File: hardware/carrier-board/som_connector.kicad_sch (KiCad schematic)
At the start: 4 parts, among them J1 SS5-80-3.50-L-D-K-TR, J2 SS5-80-3.50-L-D-K-TR, J3 SS5-80-3.50-L-D-K-TR, J4 SS5-80-3.50-L-D-K-TR

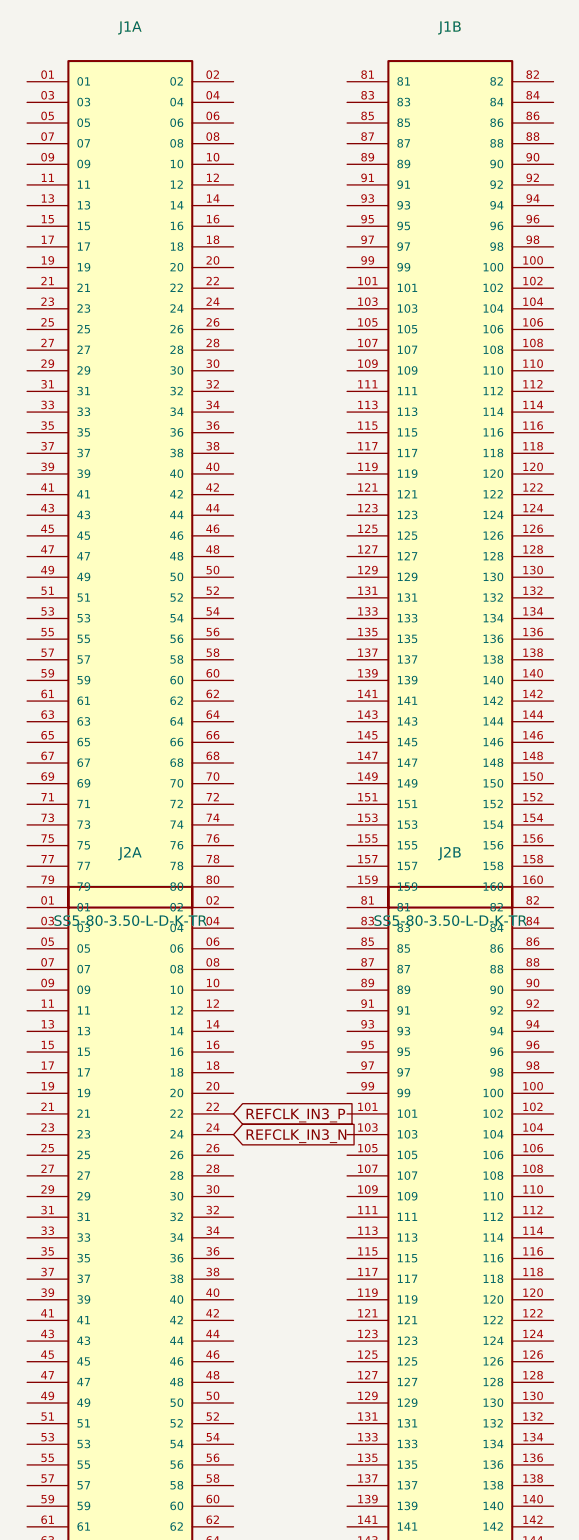
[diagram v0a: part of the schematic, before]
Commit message: Wire TMDS data lines through TI TPD1E04U04 ESD protection
Switches ESD protection from the still-blocked Semtech RClamp0574P
(6+ failed attempts, including one wrong-part PDF caught via title
metadata) to TI TPD1E04U04: a real, fully-verified, HDMI 2.0-rated
single-channel ESD diode. Fetched TI's own datasheet directly and
hand-authored the symbol/footprint from its pin function table and
mechanical land-pattern drawing (1=IO, 2=GND, X1SON/DPY0002A).

Wires all 6 TMDS data lines (D0/D1/D2, P+N) per HDMI sheet from the
connector through a dedicated ESD diode to the exact SOM connector
B2B pin resolved from the TE0807 TRM in an earlier commit. Verified
by checking every one of the 48 affected pins (24 HDMI-side, 24
SOM-side) individually against the full-hierarchy ERC report, not
just that violation counts dropped.

TMDS_CLK is deliberately left unwired: doing this work surfaced a
real architecture question this project never actually settled --
whether each input port's GTH reference clock should come from the
Si5341A (already wired in the previous commit) or from the connector's
own TMDS_CLK pair, which has real wiring and part implications either
way. Documented in carrier-board-spec.md rather than guessed at.
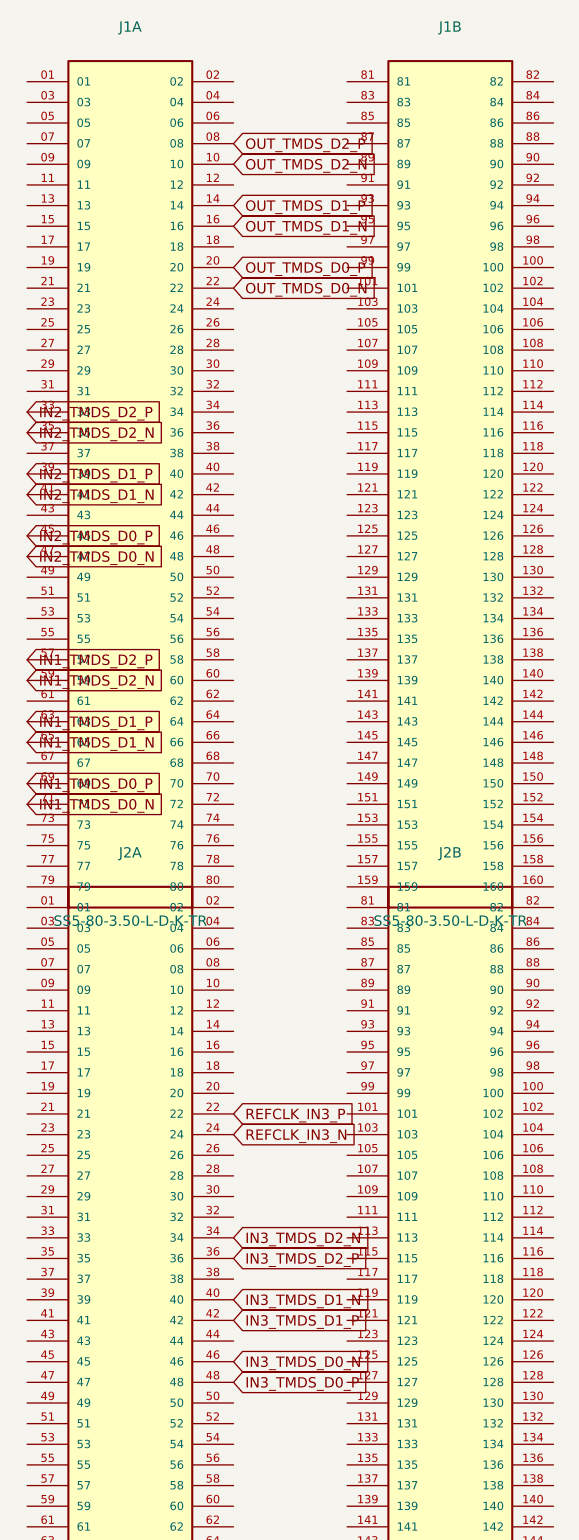
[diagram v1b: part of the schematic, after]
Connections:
- net IN3_TMDS_D2_N: now reaches J2.34
- net IN3_TMDS_D2_P: now reaches J2.36
- net IN3_TMDS_D1_N: now reaches J2.40
- net IN3_TMDS_D1_P: now reaches J2.42
- net IN3_TMDS_D0_N: now reaches J2.46
- net IN3_TMDS_D0_P: now reaches J2.48
- net OUT_TMDS_D2_P: now reaches J1.08
- net OUT_TMDS_D2_N: now reaches J1.10
- net OUT_TMDS_D1_P: now reaches J1.14
- net OUT_TMDS_D1_N: now reaches J1.16
- net OUT_TMDS_D0_P: now reaches J1.20
- net OUT_TMDS_D0_N: now reaches J1.22
- net IN2_TMDS_D2_P: now reaches J1.33
- net IN2_TMDS_D2_N: now reaches J1.35
- net IN2_TMDS_D1_P: now reaches J1.39
- net IN2_TMDS_D1_N: now reaches J1.41
- net IN2_TMDS_D0_P: now reaches J1.45
- net IN2_TMDS_D0_N: now reaches J1.47
- net IN1_TMDS_D2_P: now reaches J1.57
- net IN1_TMDS_D2_N: now reaches J1.59
- net IN1_TMDS_D1_P: now reaches J1.63
- net IN1_TMDS_D1_N: now reaches J1.65
- net IN1_TMDS_D0_P: now reaches J1.69
- net IN1_TMDS_D0_N: now reaches J1.71

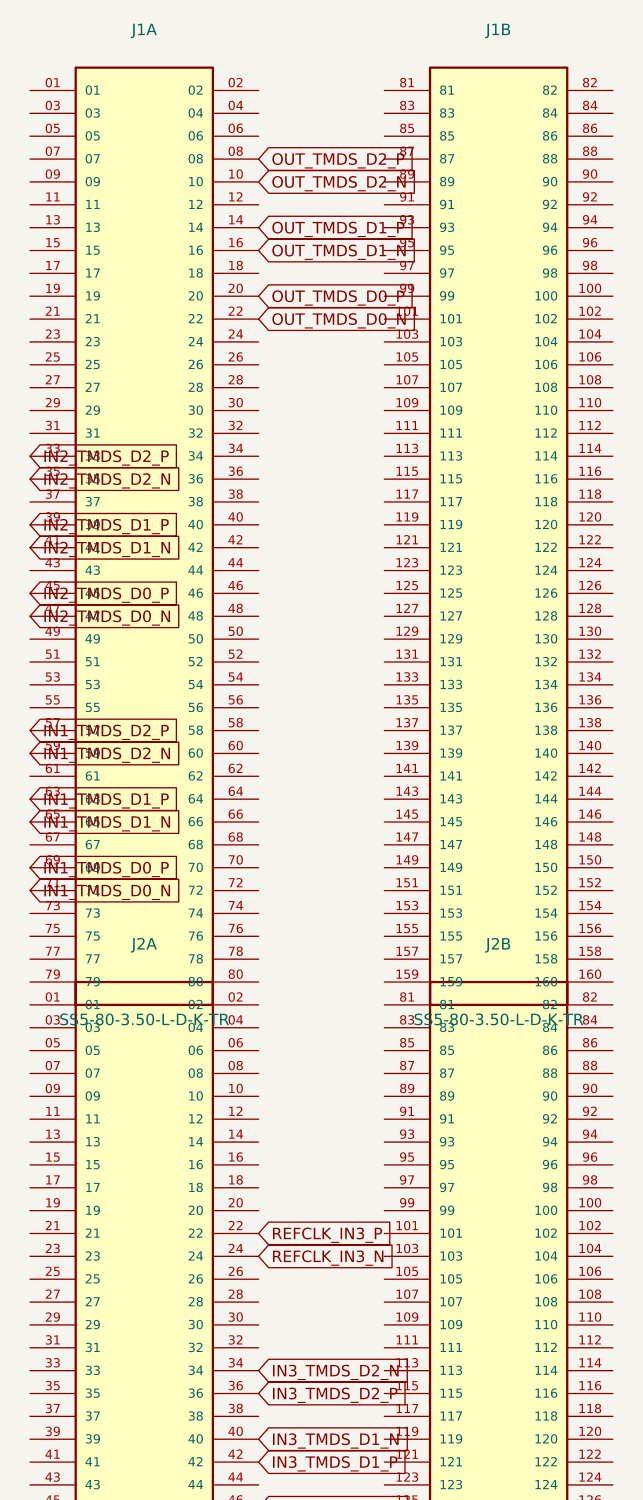
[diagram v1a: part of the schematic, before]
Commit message: Resolve TMDS_CLK routing and wire it to the spare 4th GTH lane
Researched the open question from the previous commit (per user
direction): does each input port's GTH reference clock come from
Si5341A or from the connector's own TMDS_CLK pair? AMD's own GTH
documentation (PG380) confirms the RX CDR tracks incoming data up to
+/-1250ppm from the reference-derived rate below 6.6Gb/s -- comfortably
covering our ~5.94Gbps TMDS rate -- so a single reference only needs
coarse per-format tuning, which is exactly what the Si5341A (already
wired in an earlier commit) was chosen for. TMDS_CLK itself goes to
each quad's "spare" 4th GTH lane instead, using the identical
TPD1E04U04 ESD-diode wiring pattern already validated for TMDS_DATA0-2.

No rework of prior wiring was needed. Every one of the 16 affected
pins was checked individually against the ERC report.
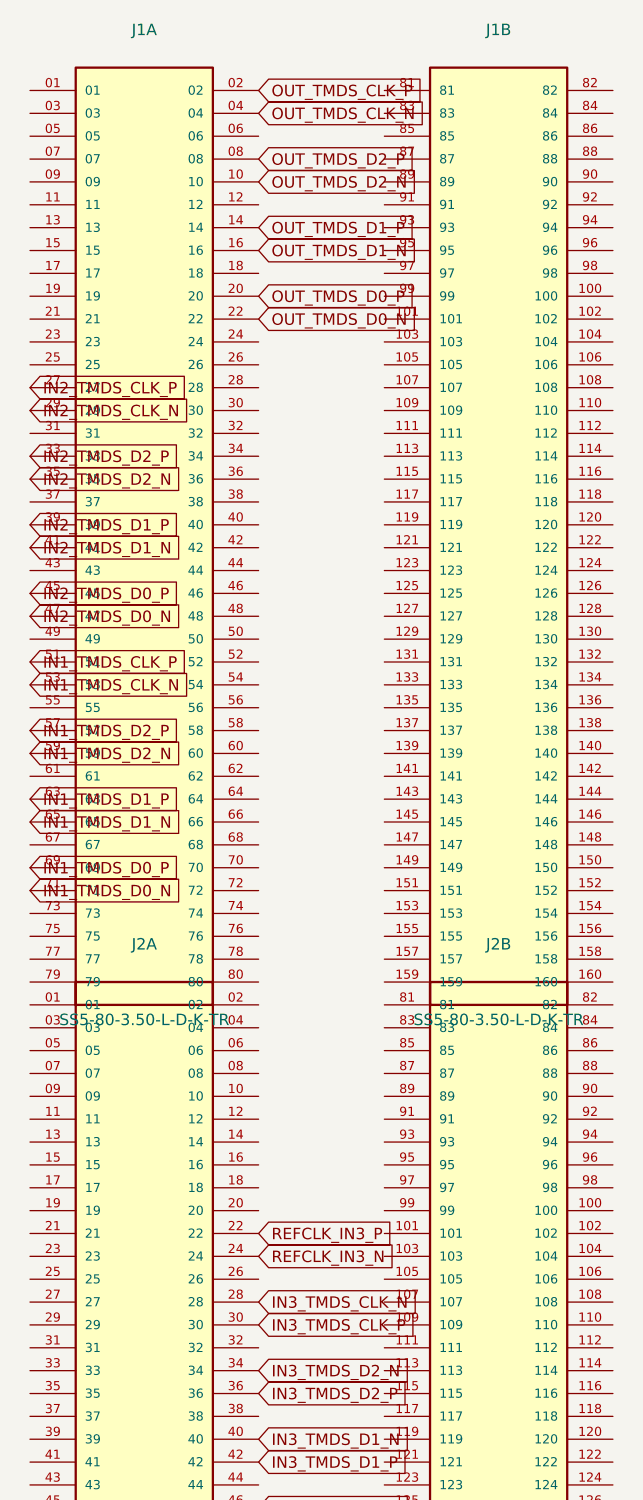
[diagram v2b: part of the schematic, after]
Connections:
- net IN3_TMDS_CLK_N: now reaches J2.28
- net IN3_TMDS_CLK_P: now reaches J2.30
- net OUT_TMDS_CLK_P: now reaches J1.02
- net OUT_TMDS_CLK_N: now reaches J1.04
- net IN2_TMDS_CLK_P: now reaches J1.27
- net IN2_TMDS_CLK_N: now reaches J1.29
- net IN1_TMDS_CLK_P: now reaches J1.51
- net IN1_TMDS_CLK_N: now reaches J1.53
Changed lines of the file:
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@@
+		)
+	)
+	(global_label "IN1_TMDS_CLK_P"
+		(shape input)
+		(at 86.36 114.3 0)
+		(fields_autoplaced yes)
+		(effects
+			(font
+				(size 1.27 1.27)
+			)
+			(justify left)
+		)
+		(property "Intersheetrefs" "${INTERSHEET_REFS}"
+			(at 86.36 114.3 0)
+			(hide yes)
+			(show_name no)
+			(do_not_autoplace no)
+			(effects
+				(font
+					(size 1.27 1.27)
+				)
+			)
+		)
+	)
+	(global_label "IN1_TMDS_CLK_N"
+		(shape input)
+		(at 86.36 116.84 0)
+		(fields_autoplaced yes)
+		(effects
+			(font
+				(size 1.27 1.27)
+			)
+			(justify left)
+		)
+		(property "Intersheetrefs" "${INTERSHEET_REFS}"
+			(at 86.36 116.84 0)
+			(hide yes)
+			(show_name no)
+			(do_not_autoplace no)
+			(effects
+				(font
+					(size 1.27 1.27)
+				)
+			)
+		)
+	)
+	(global_label "IN2_TMDS_CLK_P"
+		(shape input)
+		(at 86.36 83.82 0)
+		(fields_autoplaced yes)
+		(effects
+			(font
+				(size 1.27 1.27)
+			)
+			(justify left)
+		)
+		(property "Intersheetrefs" "${INTERSHEET_REFS}"
+			(at 86.36 83.82 0)
+			(hide yes)
+			(show_name no)
+			(do_not_autoplace no)
+			(effects
+				(font
+					(size 1.27 1.27)
+				)
+			)
+		)
+	)
+	(global_label "IN2_TMDS_CLK_N"
+		(shape input)
+		(at 86.36 86.36 0)
+		(fields_autoplaced yes)
+		(effects
+			(font
+				(size 1.27 1.27)
+			)
+			(justify left)
+		)
+		(property "Intersheetrefs" "${INTERSHEET_REFS}"
+			(at 86.36 86.36 0)
+			(hide yes)
+			(show_name no)
+			(do_not_autoplace no)
+			(effects
+				(font
+					(size 1.27 1.27)
+				)
+			)
+		)
+	)
+	(global_label "OUT_TMDS_CLK_P"
+		(shape input)
+		(at 111.76 50.8 0)
+		(fields_autoplaced yes)
+		(effects
+			(font
+				(size 1.27 1.27)
+			)
+			(justify left)
+		)
+		(property "Intersheetrefs" "${INTERSHEET_REFS}"
+			(at 111.76 50.8 0)
+			(hide yes)
+			(show_name no)
+			(do_not_autoplace no)
+			(effects
+				(font
+					(size 1.27 1.27)
+				)
+			)
+		)
+	)
+	(global_label "OUT_TMDS_CLK_N"
+		(shape input)
+		(at 111.76 53.34 0)
+		(fields_autoplaced yes)
+		(effects
+			(font
+				(size 1.27 1.27)
+			)
+			(justify left)
+		)
+		(property "Intersheetrefs" "${INTERSHEET_REFS}"
+			(at 111.76 53.34 0)
+			(hide yes)
+			(show_name no)
+			(do_not_autoplace no)
+			(effects
+				(font
+					(size 1.27 1.27)
+				)
+			)
+		)
+	)
+	(global_label "IN3_TMDS_CLK_P"
+		(shape input)
+		(at 111.76 187.96 0)
+		(fields_autoplaced yes)
+		(effects
+			(font
+				(size 1.27 1.27)
+			)
+			(justify left)
+		)
+		(property "Intersheetrefs" "${INTERSHEET_REFS}"
+			(at 111.76 187.96 0)
+			(hide yes)
+			(show_name no)
+			(do_not_autoplace no)
+			(effects
+				(font
+					(size 1.27 1.27)
+				)
+			)
+		)
+	)
+	(global_label "IN3_TMDS_CLK_N"
+		(shape input)
+		(at 111.76 185.42 0)
+		(fields_autoplaced yes)
+		(effects
+			(font
+				(size 1.27 1.27)
+			)
+			(justify left)
+		)
+		(property "Intersheetrefs" "${INTERSHEET_REFS}"
+			(at 111.76 185.42 0)
+			(hide yes)
+			(show_name no)
+			(do_not_autoplace no)
+			(effects
+				(font
+					(size 1.27 1.27)
+				)
+			)
 		)
 	)
